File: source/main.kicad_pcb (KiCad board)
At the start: 2 copper layers, 85.6 x 54 mm, 66 parts, among them P1 USB_Type_C_Receptacle_16_pin

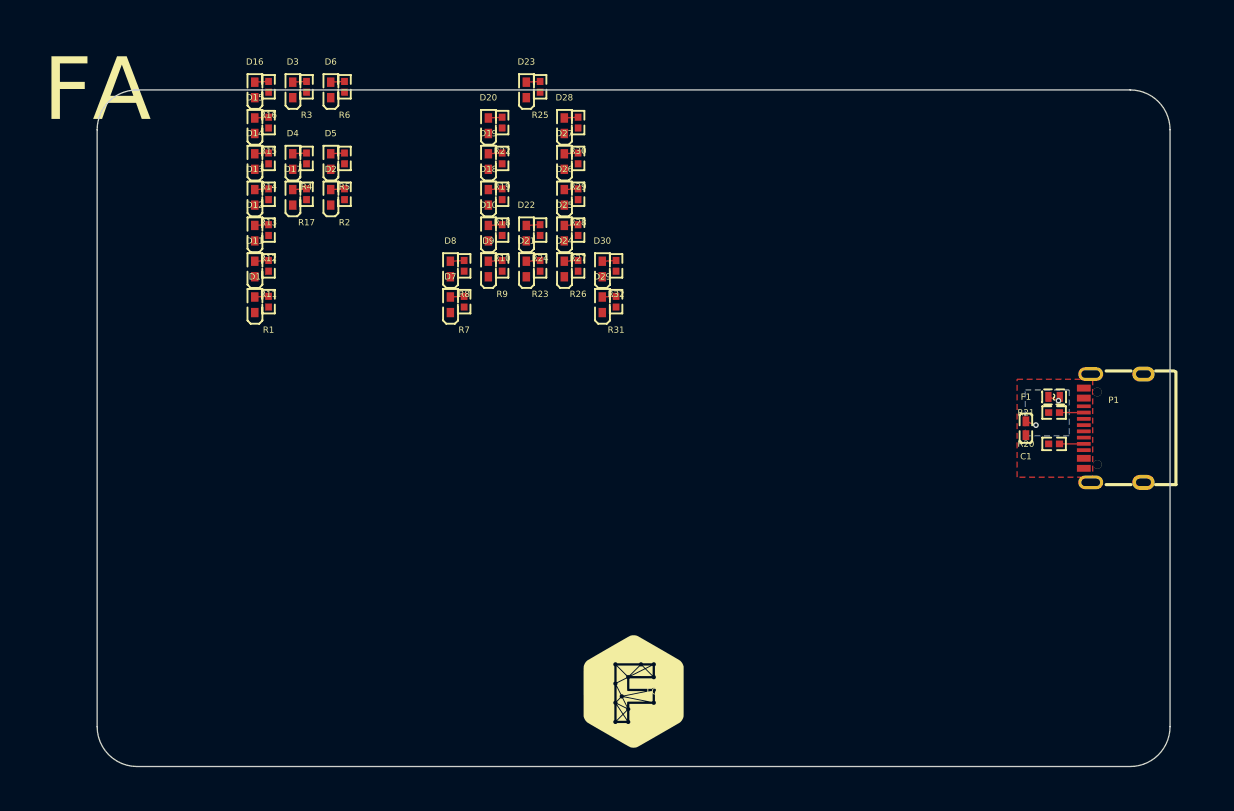
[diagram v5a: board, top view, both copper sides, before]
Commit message: Text anchor; Font downloader
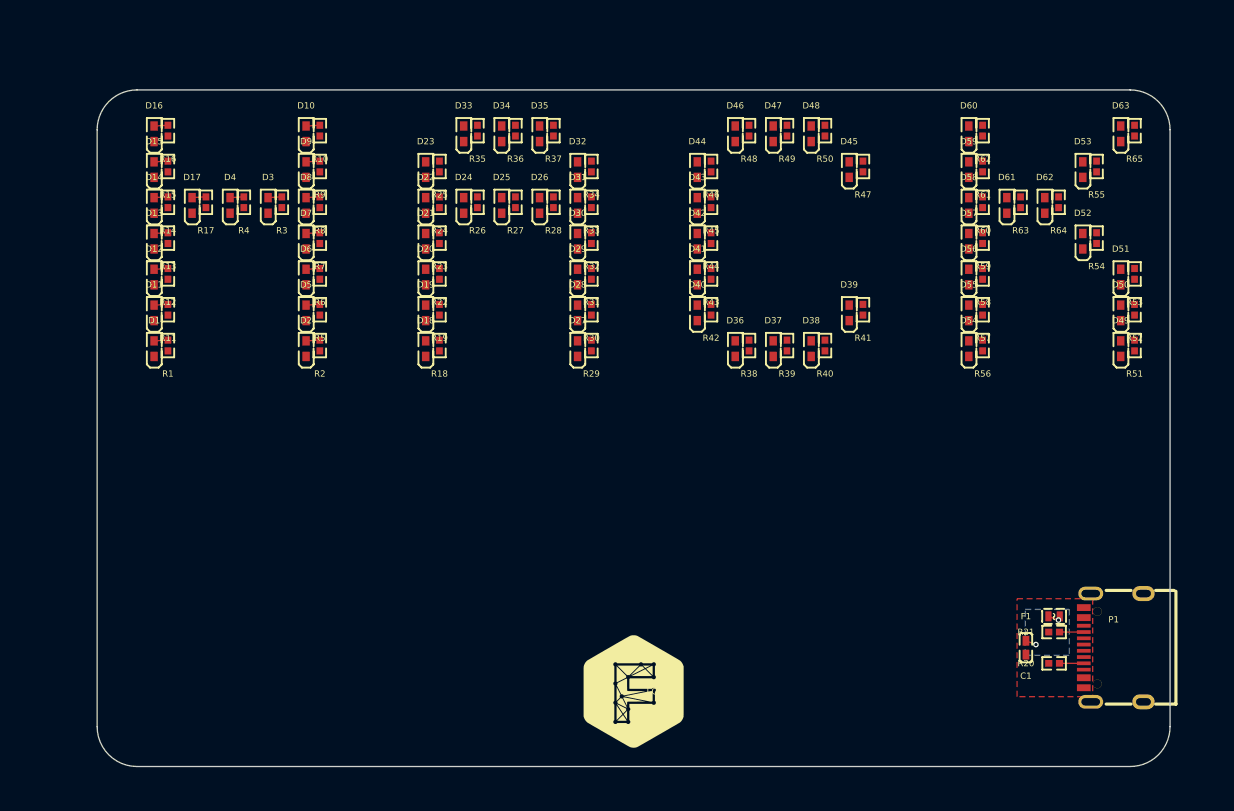
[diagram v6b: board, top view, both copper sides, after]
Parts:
- added D31: LED, lcsc:LED0402-R-RD_RED, F.Cu at (38.3, 9.21)
- added D32: LED, lcsc:LED0402-R-RD_RED, F.Cu at (38.3, 6.36)
- added D33: LED, lcsc:LED0402-R-RD_RED, F.Cu at (29.2, 3.50)
- added D34: LED, lcsc:LED0402-R-RD_RED, F.Cu at (32.3, 3.50)
- added D35: LED, lcsc:LED0402-R-RD_RED, F.Cu at (35.3, 3.50)
- added D36: LED, lcsc:LED0402-R-RD_RED, F.Cu at (50.9, 20.6)
- added D37: LED, lcsc:LED0402-R-RD_RED, F.Cu at (53.9, 20.6)
- added D38: LED, lcsc:LED0402-R-RD_RED, F.Cu at (57.0, 20.6)
- added D39: LED, lcsc:LED0402-R-RD_RED, F.Cu at (60.0, 17.8)
- added D40: LED, lcsc:LED0402-R-RD_RED, F.Cu at (47.9, 17.8)
- added D41: LED, lcsc:LED0402-R-RD_RED, F.Cu at (47.9, 14.9)
- added D42: LED, lcsc:LED0402-R-RD_RED, F.Cu at (47.9, 12.1)
- added D43: LED, lcsc:LED0402-R-RD_RED, F.Cu at (47.9, 9.21)
- added D44: LED, lcsc:LED0402-R-RD_RED, F.Cu at (47.9, 6.36)
- added D45: LED, lcsc:LED0402-R-RD_RED, F.Cu at (60.0, 6.36)
- added D46: LED, lcsc:LED0402-R-RD_RED, F.Cu at (50.9, 3.50)
- added D47: LED, lcsc:LED0402-R-RD_RED, F.Cu at (53.9, 3.50)
- added D48: LED, lcsc:LED0402-R-RD_RED, F.Cu at (57.0, 3.50)
- added D49: LED, lcsc:LED0402-R-RD_RED, F.Cu at (81.7, 20.6)
- added D50: LED, lcsc:LED0402-R-RD_RED, F.Cu at (81.7, 17.8)
- added D51: LED, lcsc:LED0402-R-RD_RED, F.Cu at (81.7, 14.9)
- added D52: LED, lcsc:LED0402-R-RD_RED, F.Cu at (78.6, 12.1)
- added D53: LED, lcsc:LED0402-R-RD_RED, F.Cu at (78.6, 6.36)
- added D54: LED, lcsc:LED0402-R-RD_RED, F.Cu at (69.5, 20.6)
- added D55: LED, lcsc:LED0402-R-RD_RED, F.Cu at (69.5, 17.8)
- added D56: LED, lcsc:LED0402-R-RD_RED, F.Cu at (69.5, 14.9)
- added D57: LED, lcsc:LED0402-R-RD_RED, F.Cu at (69.5, 12.1)
- added D58: LED, lcsc:LED0402-R-RD_RED, F.Cu at (69.5, 9.21)
- added D59: LED, lcsc:LED0402-R-RD_RED, F.Cu at (69.5, 6.36)
- added D60: LED, lcsc:LED0402-R-RD_RED, F.Cu at (69.5, 3.50)
- added D61: LED, lcsc:LED0402-R-RD_RED, F.Cu at (72.6, 9.21)
- added D62: LED, lcsc:LED0402-R-RD_RED, F.Cu at (75.6, 9.21)
- added D63: LED, lcsc:LED0402-R-RD_RED, F.Cu at (81.7, 3.50)
- added R33: 100Ω, lcsc:R0402, F.Cu at (39.4, 8.96)
- added R34: 100Ω, lcsc:R0402, F.Cu at (39.4, 6.11)
- added R35: 100Ω, lcsc:R0402, F.Cu at (30.3, 3.25)
- added R36: 100Ω, lcsc:R0402, F.Cu at (33.4, 3.25)
- added R37: 100Ω, lcsc:R0402, F.Cu at (36.4, 3.25)
- added R38: 100Ω, lcsc:R0402, F.Cu at (52.0, 20.4)
- added R39: 100Ω, lcsc:R0402, F.Cu at (55.0, 20.4)
- added R40: 100Ω, lcsc:R0402, F.Cu at (58.1, 20.4)
- added R41: 100Ω, lcsc:R0402, F.Cu at (61.1, 17.5)
- added R42: 100Ω, lcsc:R0402, F.Cu at (49.0, 17.5)
- added R43: 100Ω, lcsc:R0402, F.Cu at (49.0, 14.7)
- added R44: 100Ω, lcsc:R0402, F.Cu at (49.0, 11.8)
- added R45: 100Ω, lcsc:R0402, F.Cu at (49.0, 8.96)
- added R46: 100Ω, lcsc:R0402, F.Cu at (49.0, 6.11)
- added R47: 100Ω, lcsc:R0402, F.Cu at (61.1, 6.11)
- added R48: 100Ω, lcsc:R0402, F.Cu at (52.0, 3.25)
- added R49: 100Ω, lcsc:R0402, F.Cu at (55.0, 3.25)
- added R50: 100Ω, lcsc:R0402, F.Cu at (58.1, 3.25)
- added R51: 100Ω, lcsc:R0402, F.Cu at (82.8, 20.4)
- added R52: 100Ω, lcsc:R0402, F.Cu at (82.8, 17.5)
- added R53: 100Ω, lcsc:R0402, F.Cu at (82.8, 14.7)
- added R54: 100Ω, lcsc:R0402, F.Cu at (79.7, 11.8)
- added R55: 100Ω, lcsc:R0402, F.Cu at (79.7, 6.11)
- added R56: 100Ω, lcsc:R0402, F.Cu at (70.6, 20.4)
- added R57: 100Ω, lcsc:R0402, F.Cu at (70.6, 17.5)
- added R58: 100Ω, lcsc:R0402, F.Cu at (70.6, 14.7)
- added R59: 100Ω, lcsc:R0402, F.Cu at (70.6, 11.8)
- added R60: 100Ω, lcsc:R0402, F.Cu at (70.6, 8.96)
- added R61: 100Ω, lcsc:R0402, F.Cu at (70.6, 6.11)
- added R62: 100Ω, lcsc:R0402, F.Cu at (70.6, 3.25)
- added R63: 100Ω, lcsc:R0402, F.Cu at (73.7, 8.96)
- added R64: 100Ω, lcsc:R0402, F.Cu at (76.7, 8.96)
- added R65: 100Ω, lcsc:R0402, F.Cu at (82.8, 3.25)
- moved C1 17.5 mm to (74.1, 44.5)
- moved F1 17.5 mm to (76.3, 42.0)
- moved P1 17.5 mm to (81.1, 44.5)
- moved R20 17.5 mm to (76.3, 45.8)
- moved R21 17.5 mm to (76.3, 43.2)
- moved D9 16.6 mm to (16.7, 6.36)
- moved R9 16.6 mm to (17.8, 6.11)
- moved D10 16.6 mm to (16.7, 3.50)
- moved R10 16.6 mm to (17.8, 3.25)
- moved D6 15.1 mm to (16.7, 14.9)
- moved R6 15.1 mm to (17.8, 14.7)
- moved D27 15.0 mm to (38.3, 20.6)
- moved D28 15.0 mm to (38.3, 17.8)
- moved R29 15.0 mm to (39.4, 20.4)
- moved R30 15.0 mm to (39.4, 17.5)
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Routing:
- net D30-1-R32-1: track 1.10 -> 0.00 mm
- net D29-1-R31-1: track 1.10 -> 0.00 mm
- net D23-1-R25-1: track 1.10 -> 0.00 mm
- net D22-1-R24-1: track 1.10 -> 0.00 mm
- net D21-1-R23-1: track 1.10 -> 0.00 mm
- net D20-1-R22-1: track 1.10 -> 0.00 mm
- net D19-1-R19-1: track 1.10 -> 0.00 mm
- net D18-1-R18-1: track 1.10 -> 0.00 mm
- net D28-1-R30-1: track 1.10 -> 0.00 mm
- net D27-1-R29-1: track 1.10 -> 0.00 mm
- net D26-1-R28-1: track 1.10 -> 0.00 mm
- net D25-1-R27-1: track 1.10 -> 0.00 mm
- net D24-1-R26-1: track 1.10 -> 0.00 mm
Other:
- board text removed: "FA"

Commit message: Rerender
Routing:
- net D55-1-R57-1: track 0.00 -> 1.10 mm
- net D61-1-R63-1: track 0.00 -> 1.10 mm
- net D60-1-R62-1: track 0.00 -> 1.10 mm
- net D59-1-R61-1: track 0.00 -> 1.10 mm
- net D58-1-R60-1: track 0.00 -> 1.10 mm
- net D57-1-R59-1: track 0.00 -> 1.10 mm
- net D56-1-R58-1: track 0.00 -> 1.10 mm
- net D54-1-R56-1: track 0.00 -> 1.10 mm
- net D39-1-R41-1: track 0.00 -> 1.10 mm
- net D28-1-R30-1: track 0.00 -> 1.10 mm
- net D48-1-R50-1: track 0.00 -> 1.10 mm
- net D47-1-R49-1: track 0.00 -> 1.10 mm
- net D46-1-R48-1: track 0.00 -> 1.10 mm
- net D45-1-R47-1: track 0.00 -> 1.10 mm
- net D38-1-R40-1: track 0.00 -> 1.10 mm
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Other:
- board text added: "Name: Hat Black"
- board text added: "Tel: +31 6 42069666"
- board text added: "Url: github.com/faebryk"
- board text removed: "Name: ABC"
- board text removed: "Tel: 0612341234"
- board text removed: "Url: github.com"

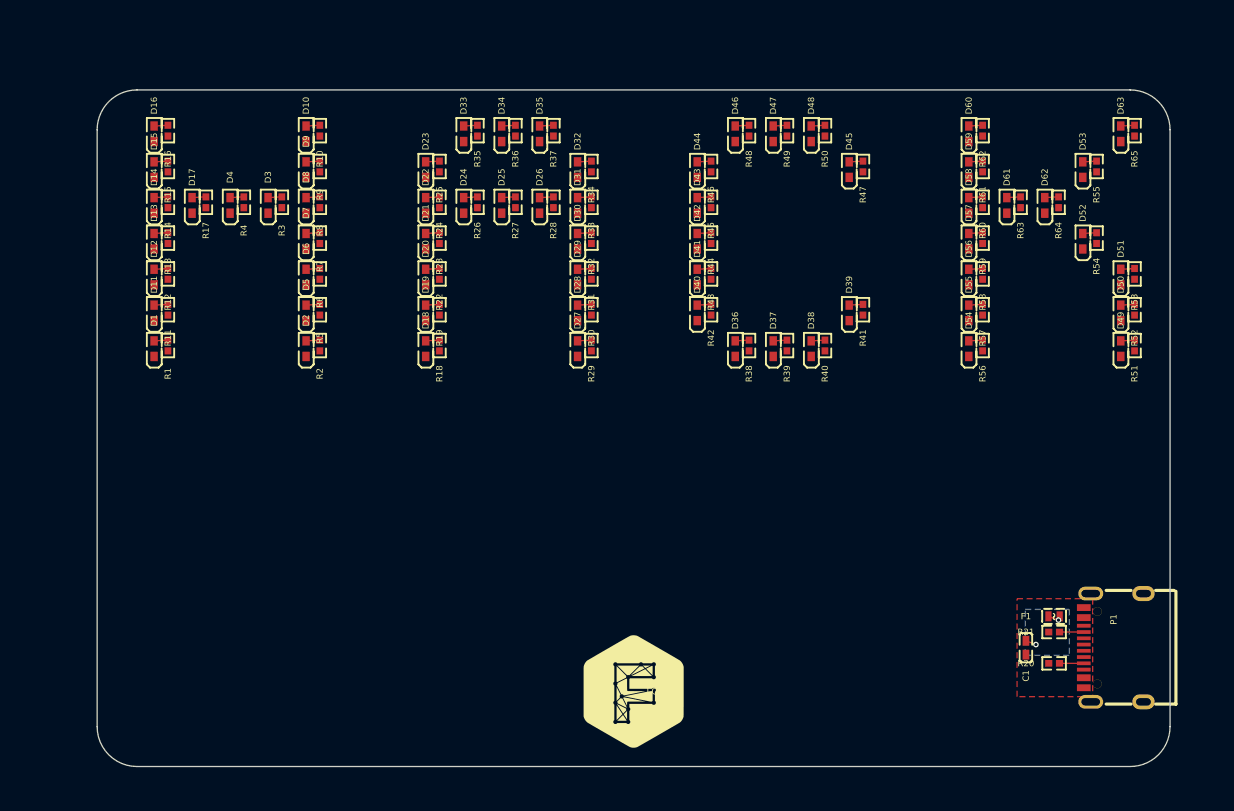
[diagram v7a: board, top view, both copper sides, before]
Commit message: Update back layout and put rpi pinout cheatsheet
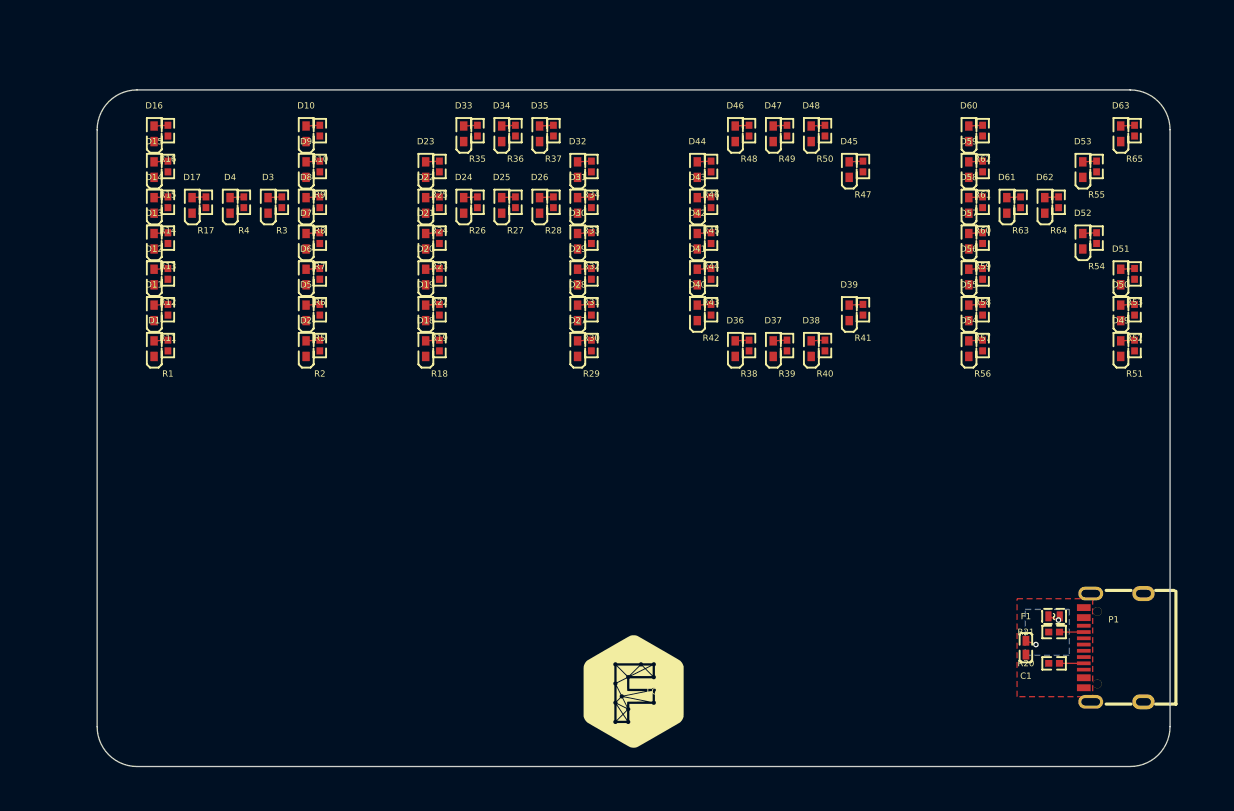
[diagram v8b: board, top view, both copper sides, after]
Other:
- board text added: "RPI PINOUT"
